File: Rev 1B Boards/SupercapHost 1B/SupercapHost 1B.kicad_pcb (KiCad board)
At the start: 2 copper layers, 40.4 x 57.8 mm, 24 parts, among them J1 XT30_F, J2 XT30_F, Q1 2SCR587D3, Q2 2SAR587D3, U1 TLV9301xDBV

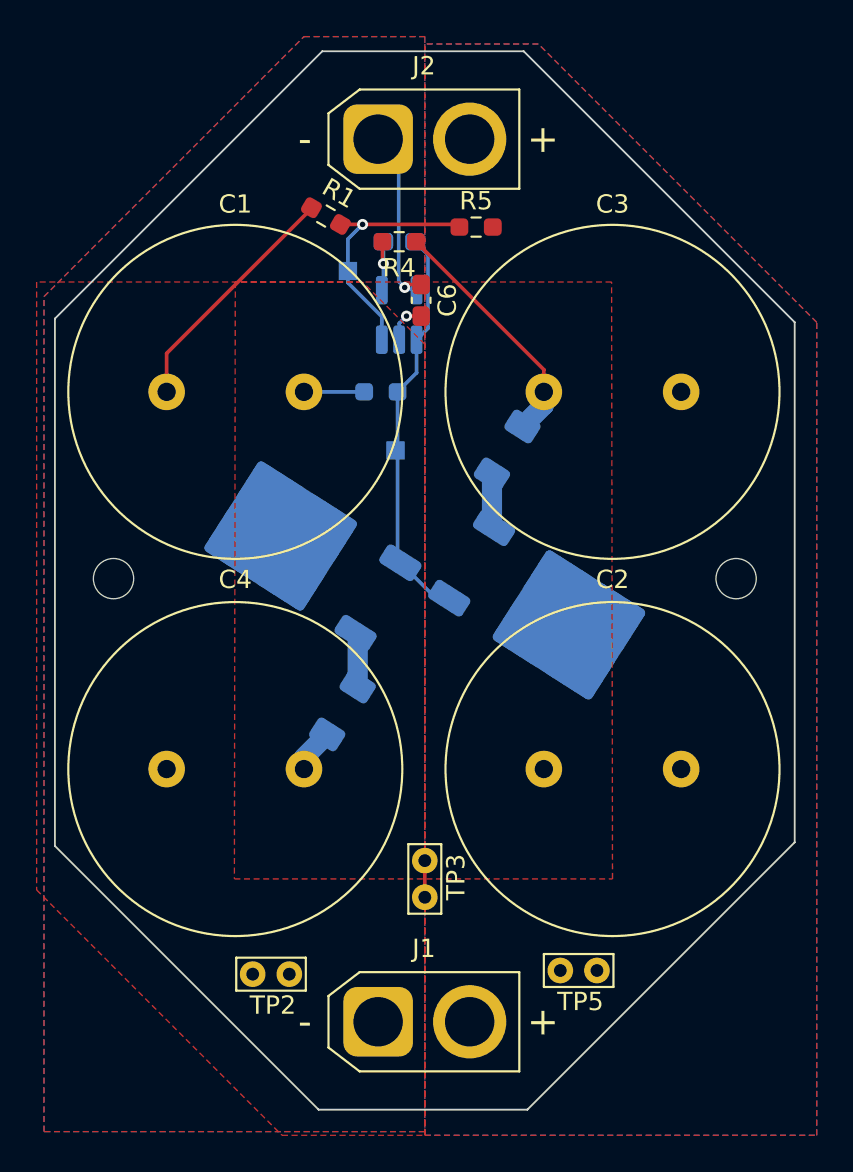
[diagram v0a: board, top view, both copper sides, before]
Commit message: Complete touchups of supercap host board
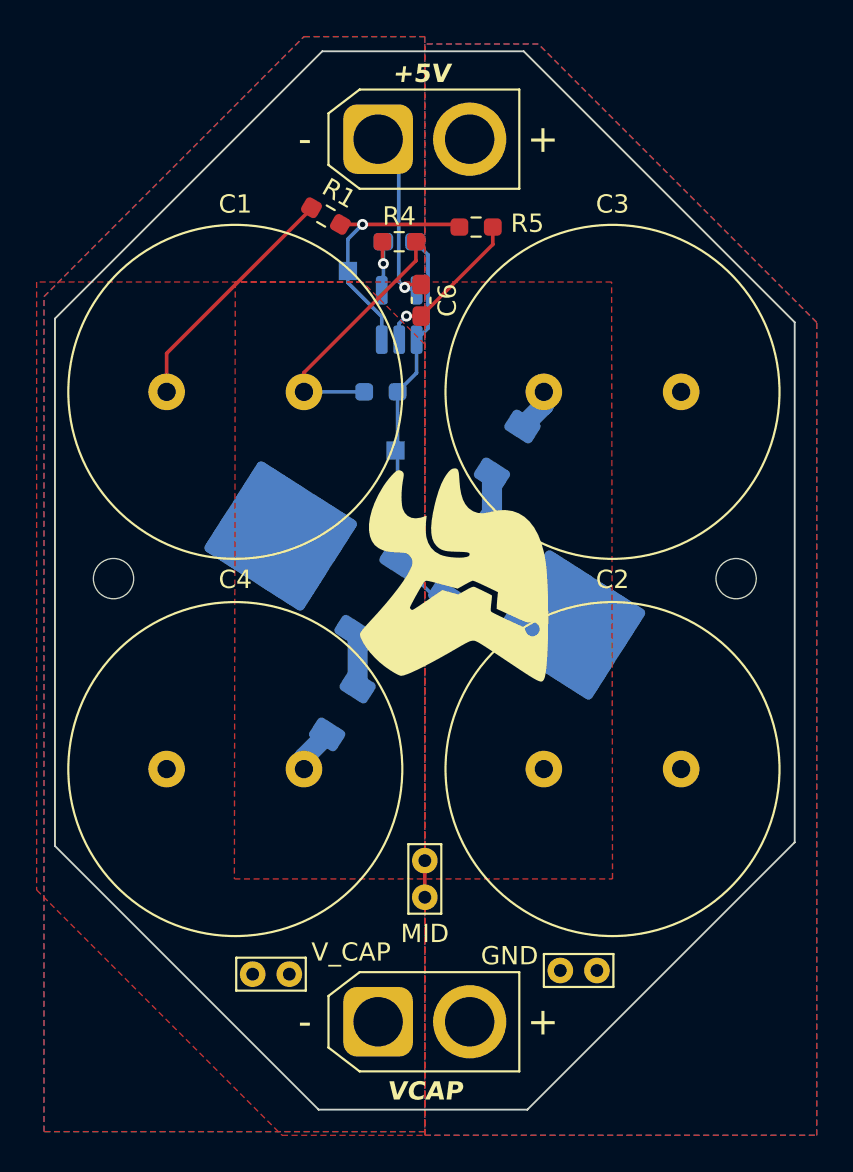
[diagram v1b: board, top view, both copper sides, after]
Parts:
- added G***: LOGO, ! Robomaster Special:StampedeLogo, F.Cu at (165.8, 104.2)
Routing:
- net GND1: track 2.25 -> 8.74 mm
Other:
- board text added: "+5V"
- board text added: "GND"
- board text added: "Jed Wang"
- board text added: "MID"
- board text added: "OP_OUT"
- board text added: "REF"
- board text added: "UT Stampede Supercapacitors"
- board text added: "VCAP"
- board text added: "V_CAP"

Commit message: Add dimensions + round corners
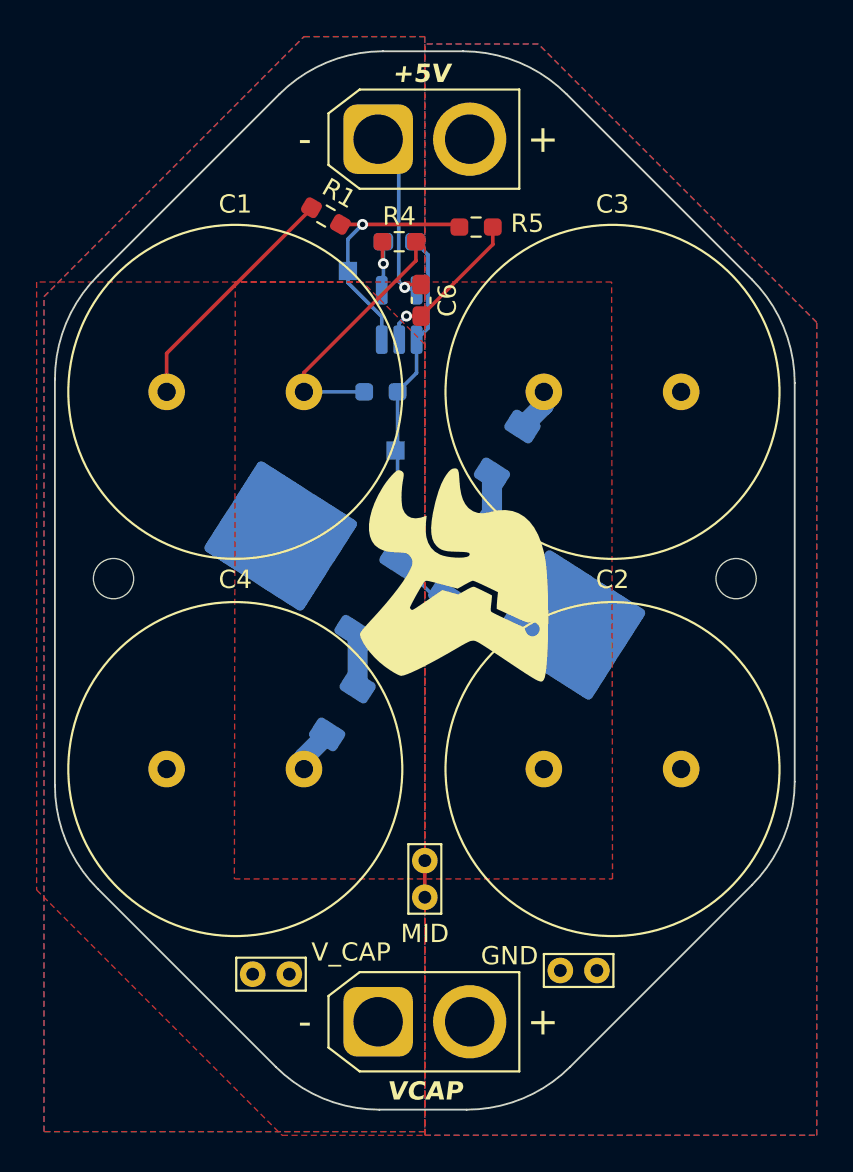
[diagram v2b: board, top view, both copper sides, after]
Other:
- outline, holes or cut-outs redrawn

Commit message: Adjust all PCBs and resize boards to be cheaper to order from JLCPCB
Also changed connector pinout to reflect silkscreen
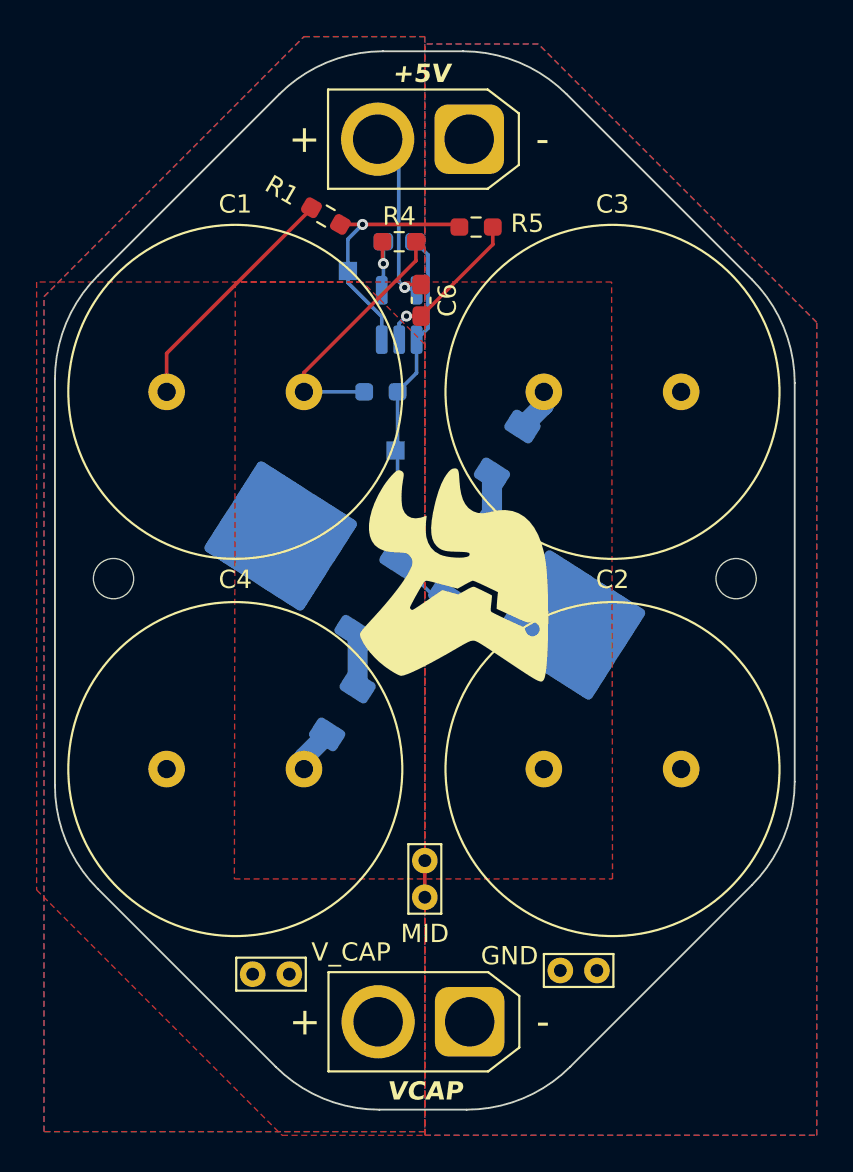
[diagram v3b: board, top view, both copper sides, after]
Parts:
- moved J1 5.00 mm to (166.7, 128.6), turned to 180 degrees
- moved J2 4.97 mm to (166.6, 80.4), turned to 180 degrees
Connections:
- J1 pad 1: /Supercapacitors/V_{CAP} -> GND1
- J1 pad 2: GND1 -> /Supercapacitors/V_{CAP}
- J2 pad 1: /Supercapacitors/V_{CC} -> GND1
- J2 pad 2: GND1 -> /Supercapacitors/V_{CC}
